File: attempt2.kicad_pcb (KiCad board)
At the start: 4 copper layers, 71.5 x 56.2 mm, 64 parts, among them J1 SIM_Card, J2 Conn_02x05_Pin, J4 USB_C_Receptacle_USB2.0_14P, Q1 PMOS, SW1 SW_DPST_x2, SW2 SW_DPST_x2, SW3 SW_Push, SW4 SW_Push, U1 nRF9160-SIxA, U2 TPD3F303DPVR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

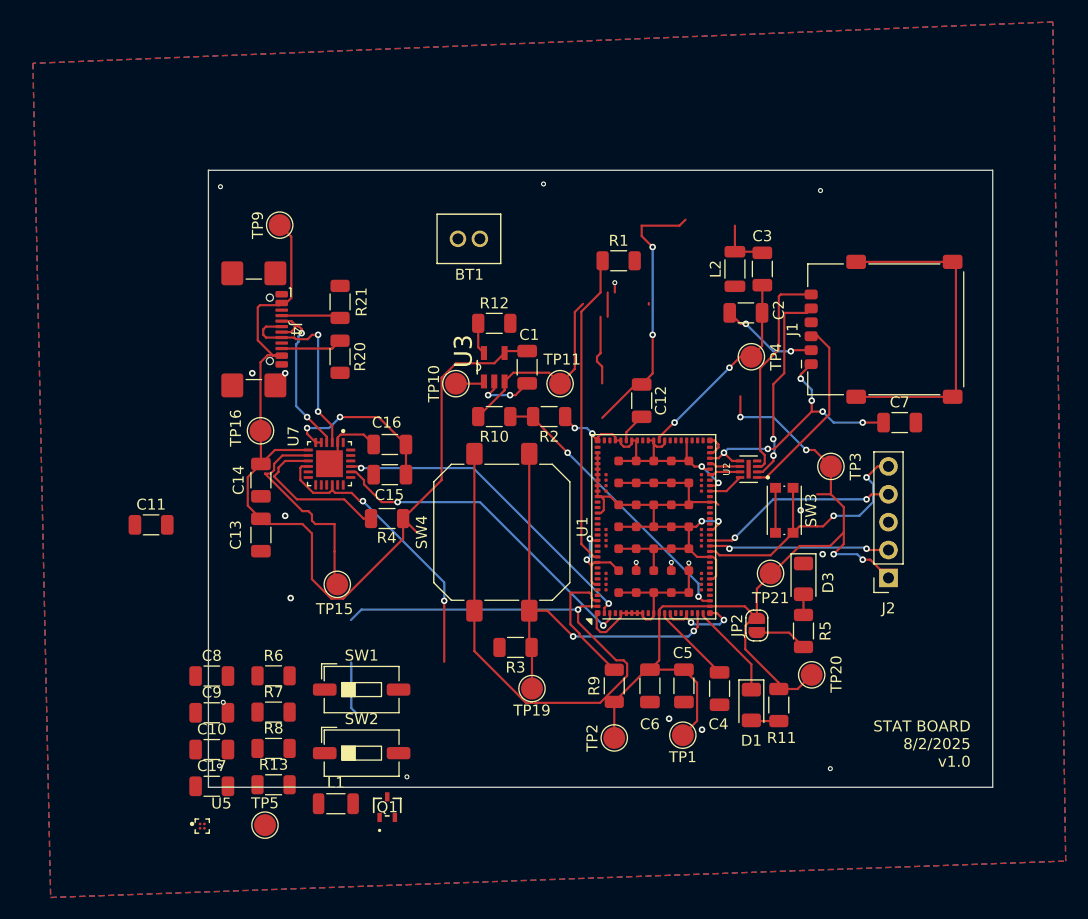
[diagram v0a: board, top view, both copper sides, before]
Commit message: remade entire pcb for new schematic
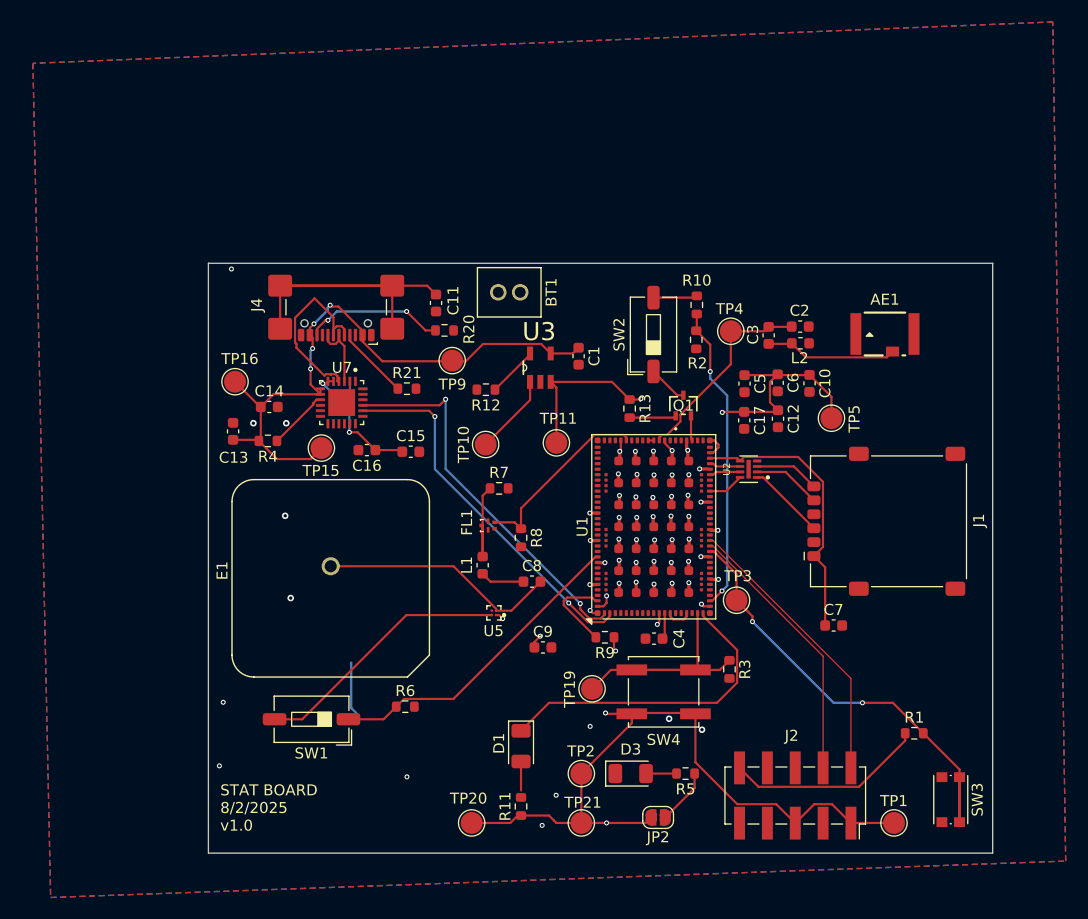
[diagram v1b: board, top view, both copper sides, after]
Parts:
- added AE1: WE-MCA_7488922455, 7488922455:WE-MCA_7488922455, F.Cu at (162.7, 93.4)
- added E1: APAE1575R1820ABDC1-T, APAE1575R1820ABDC1_T:XDCR_APAE1575R1820ABDC1-T, F.Cu at (112.2, 115.7)
- added FL1: AFS14A04-1575.42-T3, AFS14A04_1575_42_T3:FIL_AFS14A04-1575.42-T3, F.Cu at (126.5, 110.9)
- C1, C10, C11, C12, C13, C14, C15, C16, C17, C2, C3, C4, C5, C6, C7, C8, C9: footprint Capacitor_SMD:C_1206_3216Metric -> Capacitor_SMD:C_0603_1608Metric
- J2: footprint Connector_PinSocket_2.54mm:PinSocket_1x05_P2.54mm_Vertical -> Connector_PinSocket_2.54mm:PinSocket_2x05_P2.54mm_Vertical_SMD
- L1, L2: footprint Inductor_SMD:L_1206_3216Metric -> Inductor_SMD:L_0603_1608Metric
- R1, R10, R11, R12, R13, R2, R20, R21, R3, R4, R5, R6, R7, R8, R9: footprint Resistor_SMD:R_1206_3216Metric -> Resistor_SMD:R_0603_1608Metric
- SW4: footprint Button_Switch_SMD:SW_Push_1P1T_NO_CK_PTS125Sx73SMTR -> Button_Switch_SMD:SW_Push_1P1T_NO_CK_KSC6xxJ
- moved C10 63.9 mm to (155.8, 97.9), turned to -90 degrees
- moved TP5 63.6 mm to (157.8, 101.1)
- moved C17 58.9 mm to (149.8, 101.3), turned to -90 degrees
- moved R1 50.8 mm to (165.3, 129.8)
- moved R13 47.2 mm to (139.4, 100.2), turned to -90 degrees
- moved SW2 46.5 mm to (141.6, 93.5), turned to 90 degrees
- moved Q1 45.5 mm to (144.3, 100.0)
- moved TP20 33.8 mm to (125.0, 138.0)
- moved U5 32.9 mm to (127.0, 118.8), turned to 180 degrees
- moved C11 32.9 mm to (121.8, 90.6), turned to -90 degrees
- moved C9 30.8 mm to (131.5, 122.0)
- moved C8 30.4 mm to (130.5, 116.0)
- moved SW3 30.4 mm to (168.7, 135.9)
- moved C6 30.0 mm to (152.9, 97.9)
- moved R8 29.6 mm to (129.5, 112.0), turned to -90 degrees
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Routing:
- net GND: track 179.6 -> 46.8 mm, vias 34 -> 58
- net +3V8: track 197.3 -> 105.0 mm, vias 8 -> 10
- net (no net): track 63.3 -> 0.00 mm, vias 2 -> 0
- net VBUS: track 105.1 -> 58.1 mm, vias 0 -> 4
- net Net-(U1-~{RESET}): track 0.00 -> 41.6 mm, vias 0 -> 2
- net Net-(J4-SHIELD): track 0.00 -> 32.6 mm
- net Net-(SW1A-B): track 0.00 -> 23.7 mm
- net Net-(U5-RFIN): track 0.00 -> 22.0 mm
- net STATUS_LED: track 8.80 -> 29.1 mm
- net Net-(J2-Pin_10): track 0.00 -> 18.2 mm
- net USER_BTN: track 39.5 -> 24.7 mm, vias 2 -> 0
- net GPS: track 2.73 -> 17.2 mm
- net Net-(J1-I/O): track 19.9 -> 5.92 mm
- net Net-(J1-CLK): track 18.5 -> 6.24 mm, vias 2 -> 0
- net DP: track 18.0 -> 6.21 mm, vias 2 -> 0
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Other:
- board size 71.5 x 56.2 mm -> 71.5 x 53.8 mm

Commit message: updated gps antenna
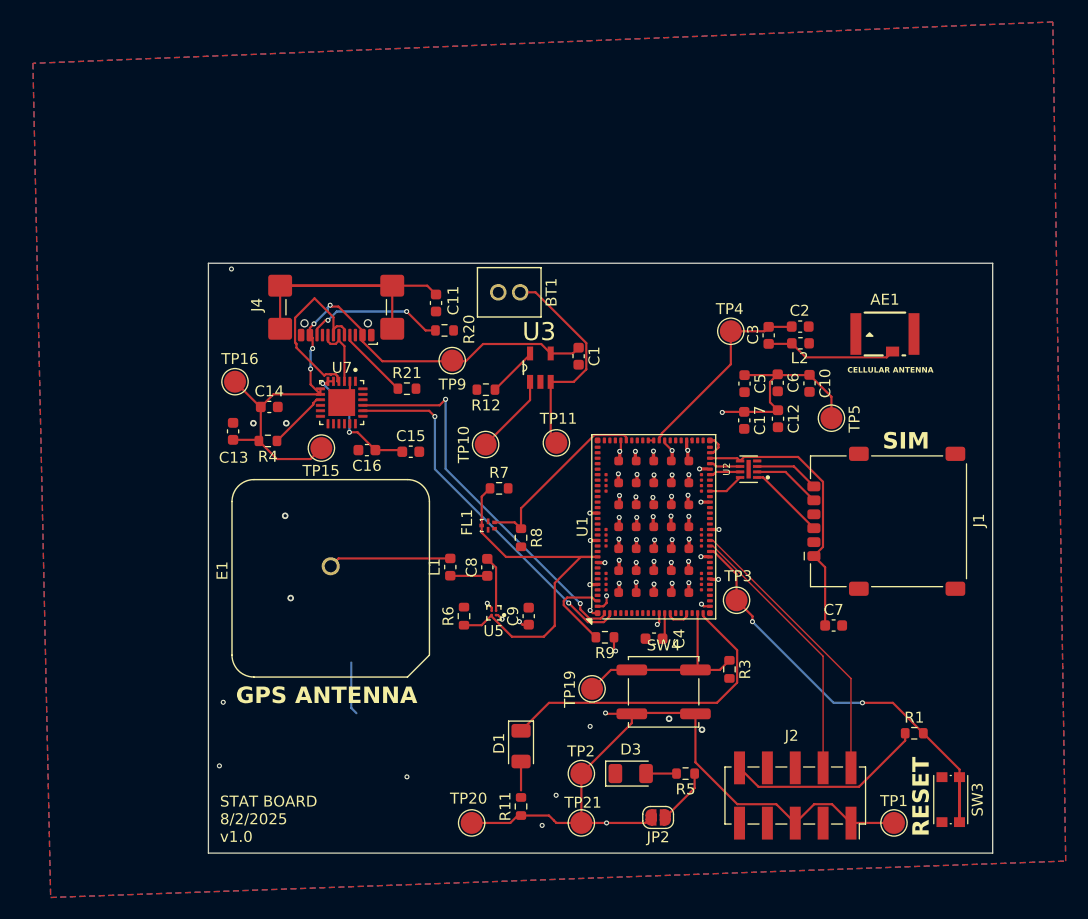
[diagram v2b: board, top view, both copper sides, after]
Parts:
- removed Q1: PMOS, footprints_mosfet:SOT-323-3_2P2X1P35_ONS-L
- removed R10, R2: 100k, Resistor_SMD:R_0603_1608Metric
- removed R13: 10k, Resistor_SMD:R_0603_1608Metric
- removed SW1, SW2: SW_DPST_x2, Button_Switch_SMD:SW_DIP_SPSTx01_Slide_6.7x4.1mm_W6.73mm_P2.54mm_LowProfile_JPin
- SW4: footprint Button_Switch_SMD:SW_Push_1P1T_NO_CK_KSC6xxJ -> Button_Switch_SMD:SW_Push_1P1T_NO_CK_KSC7xxJ
- moved R6 9.83 mm to (124.3, 119.2), turned to 90 degrees
- moved C8 4.28 mm to (126.4, 114.7), turned to 90 degrees
- moved C9 3.13 mm to (130.2, 119.2), turned to 90 degrees
- moved L1 2.96 mm to (123.0, 114.7)
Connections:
- E1 pad 1: Net-(U5-RFIN) -> Net-(E1-Pad1)
- FL1 pad C: Net-(FL1-IN) -> COEX0
- L1 pad 2: Net-(FL1-IN) -> Net-(E1-Pad1)
- R7 pad 1: Net-(FL1-IN) -> COEX0
- U1 pad 55: GPIO -> unconnected-(U1-MAGPIO0-Pad55)
- U5 pad A2: Net-(SW1A-B) -> COEX0
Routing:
- net BAT_READ: track 28.1 -> 0.00 mm, vias 2 -> 0
- net Net-(SW1A-B): track 23.7 -> 0.00 mm
- net Net-(U5-RFIN): track 22.0 -> 5.06 mm
- net Net-(E1-Pad1): track 0.00 -> 11.2 mm
- net Net-(FL1-IN): track 9.35 -> 0.00 mm
- net COEX0: track 28.8 -> 34.5 mm
- net +3V8: track 105.0 -> 109.9 mm, vias 10 -> 9
- net Net-(Q1-D): track 4.27 -> 0.00 mm
- net Net-(SW2A-B): track 4.02 -> 0.00 mm
- net Net-(Q1-S): track 3.62 -> 0.00 mm
- net GPIO: track 2.28 -> 0.00 mm
- net GND: track 46.8 -> 47.7 mm, vias 58 -> 59
- net Net-(C8-Pad1): track 4.02 -> 3.38 mm
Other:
- board text added: "CELLULAR ANTENNA"
- board text added: "GPS ANTENNA"
- board text added: "RESET"
- board text added: "SIM"

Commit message: changed nrf9160 to nrf9151
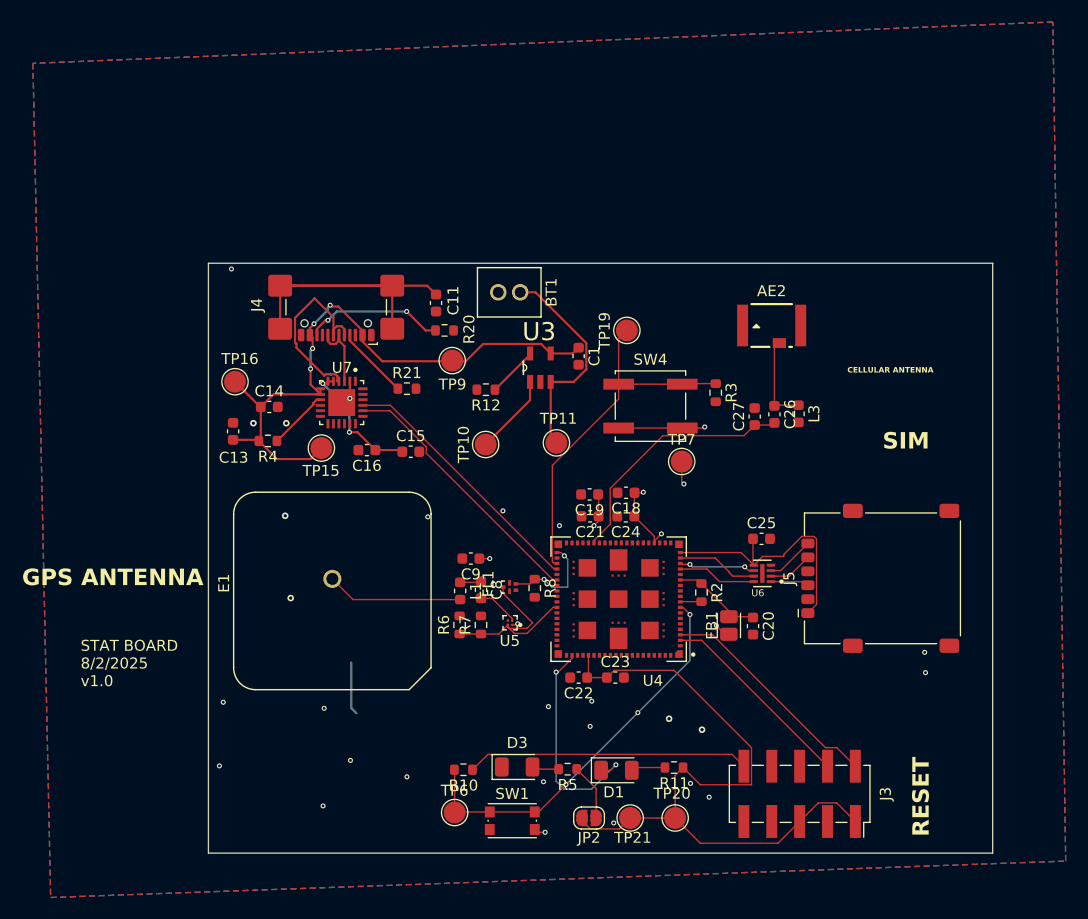
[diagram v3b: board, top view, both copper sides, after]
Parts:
- removed AE1: WE-MCA_7488922455, 7488922455:WE-MCA_7488922455
- removed C10: 47u, Capacitor_SMD:C_0603_1608Metric
- removed C12, C6: 100n, Capacitor_SMD:C_0603_1608Metric
- removed C17, C4: 4.7u, Capacitor_SMD:C_0603_1608Metric
- removed C2, C3, C5: 15p, Capacitor_SMD:C_0603_1608Metric
- removed C7: 1n, Capacitor_SMD:C_0603_1608Metric
- removed J1: SIM_Card, Connector_Card:nanoSIM_GCT_SIM8060-6-0-14-00
- removed J2: Conn_02x05_Pin, Connector_PinSocket_2.54mm:PinSocket_2x05_P2.54mm_Vertical_SMD
- removed L2: 39n, Inductor_SMD:L_0603_1608Metric
- removed R1, R9: 10k, Resistor_SMD:R_0603_1608Metric
- removed SW3: SW_Push, Button_Switch_SMD:SW_Push_1P1T_NO_CK_KMR2
- removed TP1, TP2, TP3, TP4, TP5: TestPoint, TestPoint:TestPoint_Pad_D2.0mm
- removed U1: nRF9160-SIxA, Package_LGA:Nordic_nRF9160-SIxx_LGA-102-59EP_16.0x10.5mm_P0.5mm
- removed U2: TPD3F303DPVR, TPD3F303DPVR:SON50P210X160X65-9N
- added AE2: WE-MCA_7488922455, 7488922455:WE-MCA_7488922455, F.Cu at (152.3, 92.7)
- added C18: C, Capacitor_SMD:C_0603_1608Metric, F.Cu at (139.1, 107.9)
- added C19: C, Capacitor_SMD:C_0603_1608Metric, F.Cu at (135.8, 108.0)
- added C20: C, Capacitor_SMD:C_0603_1608Metric, F.Cu at (150.7, 120.0)
- added C21: C, Capacitor_SMD:C_0603_1608Metric, F.Cu at (135.8, 110.0)
- added C22: 100n, Capacitor_SMD:C_0603_1608Metric, F.Cu at (134.8, 124.8)
- added C23: 4.7u, Capacitor_SMD:C_0603_1608Metric, F.Cu at (138.1, 124.8)
- added C24: C, Capacitor_SMD:C_0603_1608Metric, F.Cu at (139.1, 110.0)
- added C25: 1n, Capacitor_SMD:C_0603_1608Metric, F.Cu at (151.4, 112.1)
- added C26: 15p, Capacitor_SMD:C_0603_1608Metric, F.Cu at (152.6, 100.8)
- added C27: 15p, Capacitor_SMD:C_0603_1608Metric, F.Cu at (150.8, 101.0)
- added FB1: FerriteBead, Inductor_SMD:L_Eaton_MCL2012V1, F.Cu at (148.4, 120.0)
- added J3: Conn_02x05_Pin, Connector_PinSocket_2.54mm:PinSocket_2x05_P2.54mm_Vertical_SMD, F.Cu at (154.9, 135.3)
- added J5: SIM_Card, Connector_Card:nanoSIM_GCT_SIM8060-6-0-14-00, F.Cu at (162.4, 115.7)
- added L3: 39n, Inductor_SMD:L_0603_1608Metric, F.Cu at (154.8, 100.7)
- added R10: 10k, Resistor_SMD:R_0603_1608Metric, F.Cu at (124.2, 133.2)
- added R2: 10k, Resistor_SMD:R_0603_1608Metric, F.Cu at (145.9, 117.0)
- added SW1: SW_Push, Button_Switch_SMD:SW_Push_1P1T_NO_CK_KMR2, F.Cu at (128.7, 137.8)
- added TP6: TestPoint, TestPoint:TestPoint_Pad_D2.0mm, F.Cu at (123.5, 137.1)
- added TP7: TestPoint, TestPoint:TestPoint_Pad_D2.0mm, F.Cu at (144.2, 105.0)
- added U4: NRF9151-LACA-R7, NRF9151_LACA_R7:XCVR_NRF9151-LACA-R7, F.Cu at (138.4, 117.6)
- added U6: TPD3F303DPVR, TPD3F303DPVR:SON50P210X160X65-9N, F.Cu at (151.5, 115.2)
- SW4: footprint Button_Switch_SMD:SW_Push_1P1T_NO_CK_KSC7xxJ -> Button_Switch_SMD:SW_Push_1P1T_NO_CK_KSC6xxJ
- moved TP19 32.8 mm to (139.2, 93.1)
- moved SW4 26.1 mm to (141.3, 100.0)
- moved R3 25.3 mm to (147.2, 98.8)
- moved TP20 18.6 mm to (143.6, 137.6)
- moved R11 14.4 mm to (143.4, 132.9), turned to 180 degrees
- moved R7 12.6 mm to (125.8, 120.0), turned to 90 degrees
- moved R5 10.8 mm to (133.8, 133.1)
- moved D3 10.4 mm to (129.2, 132.9)
- moved D1 8.97 mm to (138.2, 133.2), turned to 0 degrees
- moved C9 7.44 mm to (124.9, 113.9), turned to 180 degrees
- moved JP2 6.30 mm to (135.7, 137.6)
- moved FL1 5.94 mm to (128.4, 116.5)
- moved R8 4.77 mm to (130.8, 116.6)
- moved TP21 4.47 mm to (139.4, 137.6)
- moved L1 2.35 mm to (124.0, 116.8), turned to -90 degrees
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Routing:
- net Net-(U1-~{RESET}): track 41.6 -> 0.00 mm, vias 2 -> 0
- net GND: track 47.7 -> 9.03 mm, vias 59 -> 27
- net Net-(U4A-~{RESET}): track 0.00 -> 36.4 mm, vias 0 -> 3
- net Net-(J2-Pin_2): track 26.2 -> 0.00 mm
- net Net-(J3-Pin_10): track 0.00 -> 25.8 mm
- net Net-(J1-VCC): track 25.4 -> 0.00 mm
- net Net-(J2-Pin_4): track 24.7 -> 0.00 mm
- net Net-(J5-VCC): track 0.00 -> 23.7 mm
- net Net-(U4A-ANT): track 0.00 -> 23.0 mm
- net Net-(J3-Pin_2): track 0.00 -> 20.9 mm
- net Net-(U1-ANT): track 18.4 -> 0.00 mm
- net Net-(J2-Pin_10): track 18.2 -> 0.00 mm
- net Net-(J3-Pin_4): track 0.00 -> 18.2 mm
- net COEX0: track 34.5 -> 17.5 mm
- net Net-(AE1-Pad3): track 12.1 -> 0.00 mm
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
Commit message: added silkscreen
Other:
- board size 71.5 x 53.8 mm -> 71.5 x 54.4 mm
- board text added: "IC"
- board text added: "USB-C"
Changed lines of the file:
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@@
 		(at 138.4 117.6 180)
 		(property "Reference" "U4"
-			(at -3.125 -7.435 0)
+			(at -3.3 -6.2 0)
 			(layer "F.SilkS")
 			(effects
@@
 		(tags "capacitor")
 		(property "Reference" "C27"
-			(at 0 -1.43 90)
+			(at 2.15 0.15 180)
 			(layer "F.SilkS")
 			(effects
@@
 		(at 113.15 99.675 -90)
 		(property "Reference" "U7"
-			(at -3.175 -0.025 180)
+			(at 0.225 -3.3 270)
 			(layer "F.SilkS")
 			(effects
@@
 		(tags "test point SMD pad")
 		(property "Reference" "TP19"
-			(at 2.025 -0.025 270)
+			(at 0 2.1 0)
 			(layer "F.SilkS")
 			(effects
@@
 		(tags "test point SMD pad")
 		(property "Reference" "TP21"
-			(at 1.8 -0.25 0)
+			(at 2.15 -0.2 0)
 			(layer "F.SilkS")
 			(effects
@@
 		(tags "resistor")
 		(property "Reference" "R3"
-			(at 0 -1.43 270)
+			(at 1.975 0 0)
 			(layer "F.SilkS")
 			(effects
@@
 		(tags "capacitor")
 		(property "Reference" "C18"
-			(at 0 -1.43 0)
+			(at 0.125 1.45 0)
 			(layer "F.SilkS")
 			(effects
@@
 		(tags "capacitor")
 		(property "Reference" "C23"
-			(at 0 -1.43 0)
+			(at 0.14058 1.55 0)
 			(layer "F.SilkS")
 			(effects
@@
 		(tags "resistor")
 		(property "Reference" "R11"
-			(at 0 -1.43 0)
+			(at -0.05 1.9 0)
 			(layer "F.SilkS")
 			(effects
@@
 		(tags "capacitor")
 		(property "Reference" "C26"
-			(at 0 -1.43 90)
+			(at 2.45 0.15 180)
 			(layer "F.SilkS")
 			(effects
@@
 		(tags "solder jumper open")
 		(property "Reference" "JP2"
-			(at 0 -1.8 0)
+			(at 0 -1.9 0)
 			(layer "F.SilkS")
 			(effects
@@
 		(tags "resistor")
 		(property "Reference" "R10"
-			(at 0 -1.43 0)
+			(at -0.05 1.7 0)
 			(layer "F.SilkS")
 			(effects
@@
 		(tags "capacitor")
 		(property "Reference" "C19"
-			(at 0 -1.43 0)
+			(at 0 1.55 0)
 			(layer "F.SilkS")
 			(effects
@@
 		(tags "test point SMD pad")
 		(property "Reference" "TP7"
-			(at 0 -1.998 0)
+			(at 2.2 -0.05 90)
 			(layer "F.SilkS")
 			(effects
@@
 	(gr_rect
 		(start 101 86.975)
-		(end 172.5 140.75)
+		(end 172.5 141.4)
 		(stroke
 			(width 0.05)
@@
 	)
 	(gr_text "STAT BOARD\n8/2/2025\nv1.0"
-		(at 89.35 125.65 0)
+		(at 102.8 139.9 0)
 		(layer "F.SilkS")
 		(effects
@@
 	)
 	(gr_text "RESET"
-		(at 166.85 139.25 90)
+		(at 125.3 141.2 0)
+		(layer "F.SilkS")
+		(effects
+			(font
+				(size 1.5 1.5)
+				(thickness 0.3)
+				(bold yes)
+			)
+			(justify left bottom)
+		)
+	)
+	(gr_text "USB-C"
+		(at 106.7 96.05 0)
 		(layer "F.SilkS")
 		(effects
@@
 	)
 	(gr_text "SIM"
-		(at 162.45 104.05 0)
+		(at 160.91 109.74 0)
 		(layer "F.SilkS")
 		(effects
@@
 	)
 	(gr_text "CELLULAR ANTENNA"
-		(at 159.25 97 0)
+		(at 148.85 95.95 0)
 		(layer "F.SilkS")
 		(effects
@@
 	)
 	(gr_text "GPS ANTENNA"
-		(at 84 116.5 0)
+		(at 103.6 128.35 0)
+		(layer "F.SilkS")
+		(effects
+			(font
+				(size 1.5 1.5)
+				(thickness 0.3)
+				(bold yes)
+			)
+			(justify left bottom)
+		)
+	)
+	(gr_text "IC"
+		(at 140.7 111.7 0)
 		(layer "F.SilkS")
 		(effects
